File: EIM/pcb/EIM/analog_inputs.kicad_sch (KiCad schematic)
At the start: 30 parts

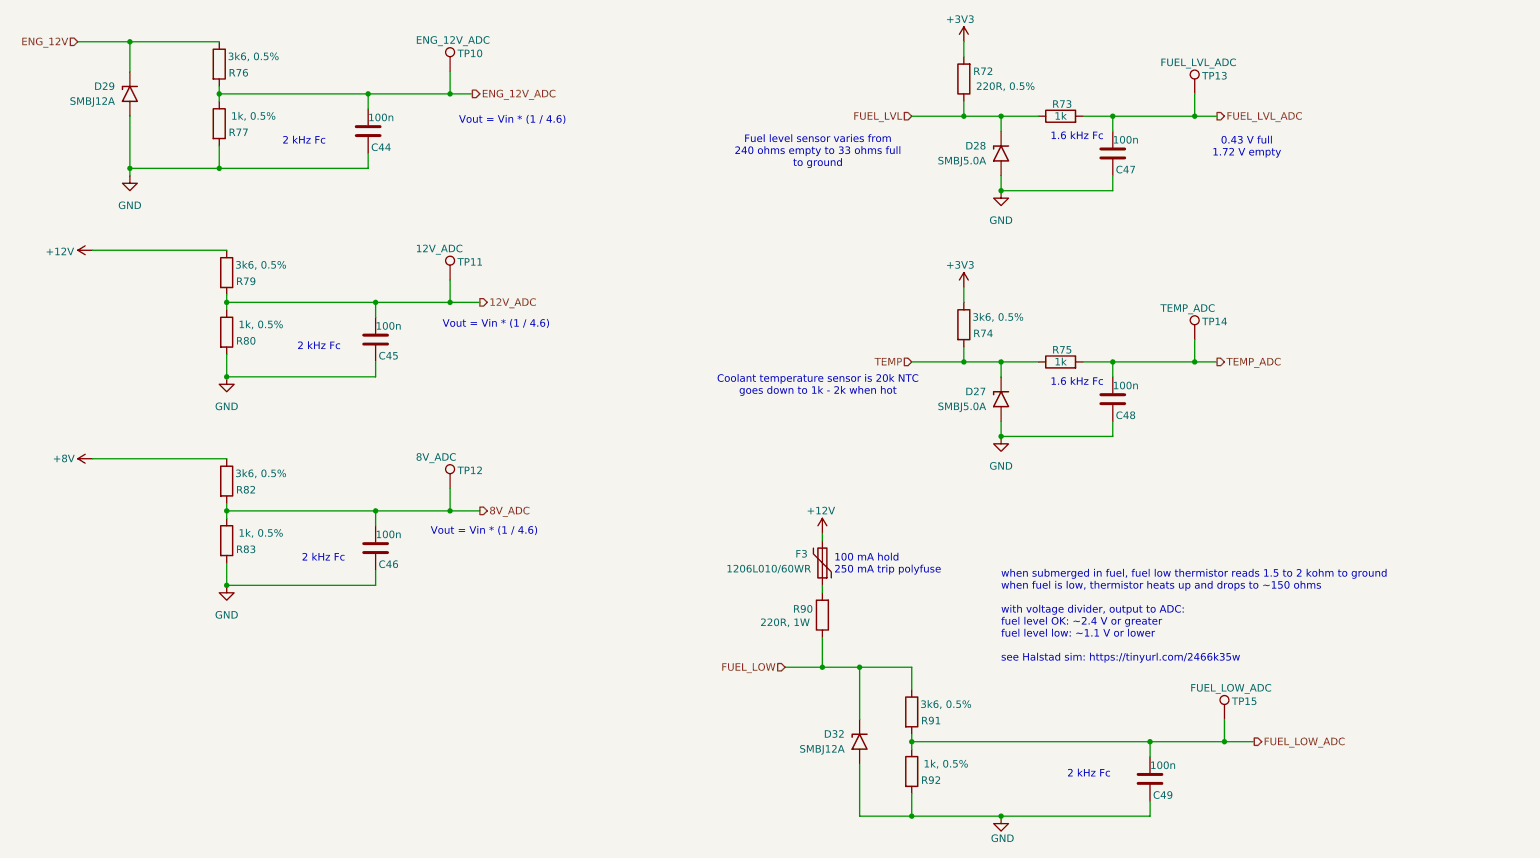
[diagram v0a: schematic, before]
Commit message: Layout 75% done, before 8V bus deletion
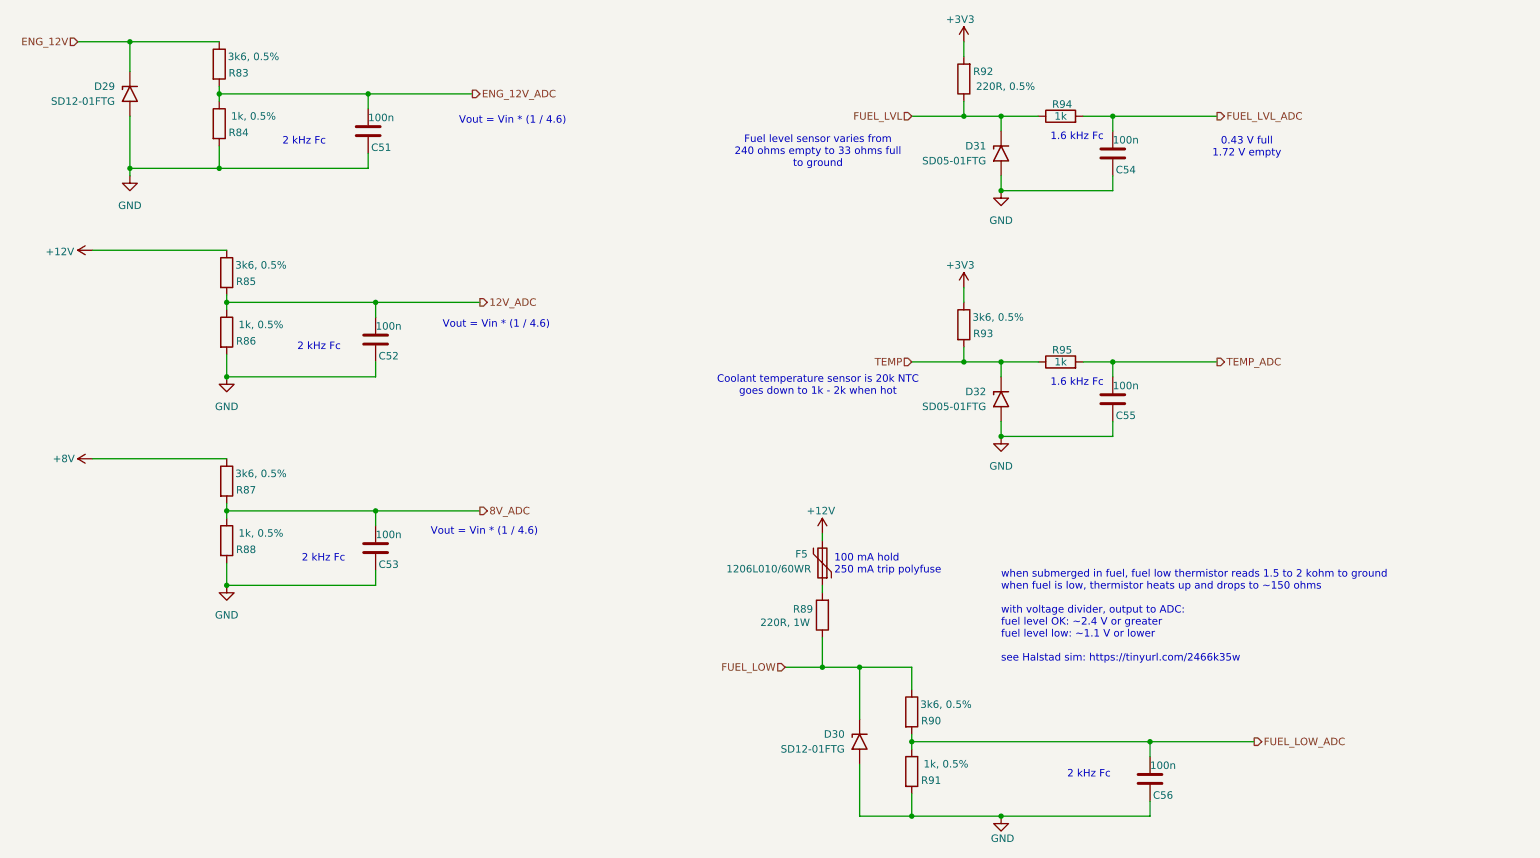
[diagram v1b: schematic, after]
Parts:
- removed TP10: ENG_12V_ADC, TestPoint:TestPoint_Pad_D1.5mm, symbol Connector:TestPoint
- removed TP11: 12V_ADC, TestPoint:TestPoint_Pad_D1.5mm, symbol Connector:TestPoint
- removed TP12: 8V_ADC, TestPoint:TestPoint_Pad_D1.5mm, symbol Connector:TestPoint
- removed TP13: FUEL_LVL_ADC, TestPoint:TestPoint_Pad_D1.5mm, symbol Connector:TestPoint
- removed TP14: TEMP_ADC, TestPoint:TestPoint_Pad_D1.5mm, symbol Connector:TestPoint
- removed TP15: FUEL_LOW_ADC, TestPoint:TestPoint_Pad_D1.5mm, symbol Connector:TestPoint
- D29: value SMBJ12A -> SD12-01FTG; footprint Diode_SMD:D_SMB -> Diode_SMD:D_SOD-323
- D30: renamed from D32; value SMBJ12A -> SD12-01FTG; footprint Diode_SMD:D_SMB -> Diode_SMD:D_SOD-323
- D31: renamed from D28; value SMBJ5.0A -> SD05-01FTG; footprint Diode_SMD:D_SMB -> Diode_SMD:D_SOD-323
- D32: renamed from D27; value SMBJ5.0A -> SD05-01FTG; footprint Diode_SMD:D_SMB -> Diode_SMD:D_SOD-323
- renumbered C44 to C51, C45 to C52, C46 to C53, C47 to C54, C48 to C55, C49 to C56, F3 to F5, R76 to R83, R77 to R84, R79 to R85, R80 to R86, R82 to R87, R83 to R88, R90 to R89, R91 to R90, R92 to R91, R72 to R92, R74 to R93, R73 to R94, R75 to R95

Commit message: All components placed and pins assigned.
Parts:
- removed C53: 100n, Capacitor_SMD:C_0805_2012Metric_Pad1.18x1.45mm_HandSolder, symbol Device:C
- removed R87: 3k6, 0.5%, Resistor_SMD:R_0805_2012Metric_Pad1.20x1.40mm_HandSolder, symbol Device:R
- removed R88: 1k, 0.5%, Resistor_SMD:R_0805_2012Metric_Pad1.20x1.40mm_HandSolder, symbol Device:R
- added C45: 100n, Capacitor_SMD:C_0805_2012Metric_Pad1.18x1.45mm_HandSolder, symbol Device:C
- added R80: 3k6, 0.5%, Resistor_SMD:R_0805_2012Metric_Pad1.20x1.40mm_HandSolder, symbol Device:R
- added R81: 1k, 0.5%, Resistor_SMD:R_0805_2012Metric_Pad1.20x1.40mm_HandSolder, symbol Device:R
- renumbered C51 to C43, C52 to C44, C54 to C46, C55 to C47, C56 to C48, D29 to D26, D30 to D27, D31 to D28, D32 to D29, R83 to R76, R84 to R77, R85 to R78, R86 to R79, R89 to R82, R90 to R83, R91 to R84, R92 to R85, R93 to R86, R94 to R87, R95 to R88
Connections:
- net GND: now also C45.2, R81.2
- new net SERVO_12V: R80.1
- new net SERVO_12V_ADC: C45.1, R80.2, R81.1
